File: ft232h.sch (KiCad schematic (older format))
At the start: 24 parts, among them P3 CONN_11, P4 CONN_11, P5 CONN_4, P6 CONN_4, P7 CONN_6, P8 CONN_4, Q1 CRYSTAL32-SMD, U3 FT232H, U4 USB-MINIB-5PIN_USB-MINIB, U5 93LC56CX-X/SN_SOIC8-N_MC

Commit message: crystal lib added , fixed mini-usb
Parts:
- removed Q1: CRYSTAL32-SMD, SparkFun-CRYSTAL-32KHZ-SMD, symbol CRYSTAL32-SMD
- removed U4: USB-MINIB-5PIN_USB-MINIB, symbol USB-MINIB-5PIN_USB-MINIB
- added CON1: USB-MINI-B, symbol USB-MINI-B
- added X1: 12MHz, ~, symbol CRYSTAL
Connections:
- wire segments 116 -> 107
- no-connect marks 0 -> 2
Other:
- moved on the sheet: C6
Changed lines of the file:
@@
-EESchema Schematic File Version 2  date 01-08-2013 14:43:33
+EESchema Schematic File Version 2
 LIBS:power
 LIBS:device
@@
 LIBS:93lc56c
 LIBS:cc3000-ft232h-cache
-EELAYER 27 0
+EELAYER 24 0
 EELAYER END
 $Descr A4 11693 8268
@@
 Wire Wire Line
 	4350 3500 4650 3500
-Text Label 4300 3400 0    60   ~ 0
+Text Label 4350 3400 0    60   ~ 0
 USB_D-
-Text Label 4300 3500 0    60   ~ 0
+Text Label 4350 3500 0    60   ~ 0
 USB_D+
 $Comp
@@
 	3950 5450 3950 5350
 $Comp
-L CRYSTAL32-SMD Q1
-U 1 1 51F9779C
-P 3400 4750
-F 0 "Q1" H 3500 4790 50  0000 L BNN
-F 1 "CRYSTAL32-SMD" H 3500 4650 50  0000 L BNN
-F 2 "SparkFun-CRYSTAL-32KHZ-SMD" H 3400 4900 50  0001 C CNN
-F 3 "~" H 3400 4750 60  0000 C CNN
-	1    3400 4750
-	1    0    0    -1
-$EndComp
-$Comp
 L C C7
 U 1 1 51F977A9
 P 3500 4950
-F 0 "C7" H 3500 5050 40  0000 L CNN
+F 0 "C7" H 3650 4900 40  0000 L CNN
 F 1 "27p" H 3506 4865 40  0000 L CNN
 F 2 "~" H 3538 4800 30  0000 C CNN
@@
 L C C6
 U 1 1 51F977AF
-P 3300 4950
-F 0 "C6" H 3300 5050 40  0000 L CNN
-F 1 "27p" H 3306 4865 40  0000 L CNN
-F 2 "~" H 3338 4800 30  0000 C CNN
-F 3 "~" H 3300 4950 60  0000 C CNN
-	1    3300 4950
+P 2900 4950
+F 0 "C6" H 2700 4950 40  0000 L CNN
+F 1 "27p" H 2906 4865 40  0000 L CNN
+F 2 "~" H 2938 4800 30  0000 C CNN
+F 3 "~" H 2900 4950 60  0000 C CNN
+	1    2900 4950
 	1    0    0    -1
 $EndComp
@@
 L GND #PWR041
 U 1 1 51F977BB
-P 3300 5150
-F 0 "#PWR041" H 3300 5150 30  0001 C CNN
-F 1 "GND" H 3300 5080 30  0001 C CNN
-F 2 "" H 3300 5150 60  0000 C CNN
-F 3 "" H 3300 5150 60  0000 C CNN
-	1    3300 5150
-	1    0    0    -1
-$EndComp
-Wire Wire Line
-	3300 4750 3300 4500
-Wire Wire Line
-	3300 4500 4650 4500
+P 2900 5150
+F 0 "#PWR041" H 2900 5150 30  0001 C CNN
+F 1 "GND" H 2900 5080 30  0001 C CNN
+F 2 "" H 2900 5150 60  0000 C CNN
+F 3 "" H 2900 5150 60  0000 C CNN
+	1    2900 5150
+	1    0    0    -1
+$EndComp
+Wire Wire Line
+	2900 4500 4650 4500
 Wire Wire Line
 	4650 4600 3500 4600
@@
 	-1   0    0    -1
 $EndComp
-Connection ~ 3300 4750
+Connection ~ 2900 4750
 Connection ~ 3500 4750
 Connection ~ 4350 5350
@@
 	1    0    0    -1
 $EndComp
-Wire Wire Line
-	1000 3150 1550 3150
-Wire Wire Line
-	1000 3150 1000 3300
-Wire Wire Line
-	800  2550 1250 2550
-Wire Wire Line
-	800  2700 1150 2700
-Wire Wire Line
-	800  2850 1150 2850
-Wire Wire Line
-	2150 2350 2150 3300
-Connection ~ 2150 2700
-Connection ~ 2150 3000
 $Comp
 L GND #PWR043
 U 1 1 51F9A1C1
-P 2150 3300
-F 0 "#PWR043" H 2150 3300 30  0001 C CNN
-F 1 "GND" H 2150 3230 30  0001 C CNN
-F 2 "" H 2150 3300 60  0000 C CNN
-F 3 "" H 2150 3300 60  0000 C CNN
-	1    2150 3300
-	1    0    0    -1
-$EndComp
-Connection ~ 2150 3150
-Text Label 800  2550 0    60   ~ 0
+P 2350 3300
+F 0 "#PWR043" H 2350 3300 30  0001 C CNN
+F 1 "GND" H 2350 3230 30  0001 C CNN
+F 2 "" H 2350 3300 60  0000 C CNN
+F 3 "" H 2350 3300 60  0000 C CNN
+	1    2350 3300
+	1    0    0    -1
+$EndComp
+Text Label 1250 2500 2    60   ~ 0
 VBUS
-Text Label 800  2700 0    60   ~ 0
-USB_D-
-Text Label 800  2850 0    60   ~ 0
+Text Label 1250 2800 2    60   ~ 0
 USB_D+
-$Comp
-L USB-MINIB-5PIN_USB-MINIB U4
-U 1 1 51FA0CB9
-P 1350 2950
-F 0 "U4" H 1350 2950 60  0001 C CNN
-F 1 "USB-MINIB-5PIN_USB-MINIB" H 1350 2950 60  0001 C CNN
-F 2 "" H 1350 2950 60  0000 C CNN
-F 3 "" H 1350 2950 60  0000 C CNN
-	1    1350 2950
-	1    0    0    -1
-$EndComp
-Connection ~ 1450 3150
-Wire Wire Line
-	1450 2350 2150 2350
-Connection ~ 1550 2350
-Wire Wire Line
-	1150 2700 1150 2650
-Wire Wire Line
-	1150 2650 1250 2650
-Wire Wire Line
-	1150 2850 1150 2750
-Wire Wire Line
-	1150 2750 1250 2750
-Wire Wire Line
-	1250 2950 1250 3150
-Connection ~ 1250 3150
 $Comp
 L 93LC56CX-X/SN_SOIC8-N_MC U5
 U 1 1 51FA6460
 P 2650 6800
-F 0 "U5" H 2650 6800 0   0001 C CNN
-F 1 "93LC56CX-X/SN_SOIC8-N_MC" H 2650 6800 0   0001 C CNN
+F 0 "U5" H 2650 6800 60  0001 C CNN
+F 1 "93LC56CX-X/SN_SOIC8-N_MC" H 2650 6800 60  0001 C CNN
 F 2 "" H 2650 6800 60  0000 C CNN
 F 3 "" H 2650 6800 60  0000 C CNN
@@
 	1    0    0    -1
 $EndComp
+Wire Wire Line
+	1000 3300 1000 3100
+NoConn ~ 1250 2950
+$Comp
+L CRYSTAL X1
+U 1 1 51FA7E94
+P 3200 4750
+F 0 "X1" H 3200 4900 60  0000 C CNN
+F 1 "12MHz" H 3200 4600 60  0000 C CNN
+F 2 "~" H 3200 4750 60  0000 C CNN
+F 3 "~" H 3200 4750 60  0000 C CNN
+	1    3200 4750
+	1    0    0    -1
+$EndComp
+Wire Wire Line
+	2900 4500 2900 4750
+NoConn ~ 2550 6700
+Text Label 1250 2650 2    60   ~ 0
+USB_D-
+Wire Wire Line
+	1000 3100 1250 3100
+$Comp
+L USB-MINI-B CON1
+U 1 1 51FA7F63
+P 1800 2800
+F 0 "CON1" H 1550 3250 60  0000 C CNN
+F 1 "USB-MINI-B" H 1750 2300 60  0000 C CNN
+F 2 "" H 1800 2800 60  0000 C CNN
+F 3 "" H 1800 2800 60  0000 C CNN
+	1    1800 2800
+	1    0    0    -1
+$EndComp
+Wire Wire Line
+	2350 2500 2350 3300
+Connection ~ 2350 3100
+Connection ~ 2350 2950
+Connection ~ 2350 2650
 $EndSCHEMATC

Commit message: updated
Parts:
- removed L1: INDUCTOR_SMALL, ~, symbol INDUCTOR_SMALL
- added C15: 4.7u, ~, symbol C
- added C16: 0.1, ~, symbol C
- added FB1, FB2, FB3: FILTER, ~, symbol FILTER
- added R4, R5, R6: 10K, ~, symbol R
- C12, C14: value 0.01 -> 4.7u
- C5: value 0.1 -> 0.01
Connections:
- net labels added: VCC3V3, VCCIO, VCORE
- net labels removed: +3.3V, VDEVICE
- wire segments 107 -> 122
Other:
- moved on the sheet: C5

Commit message: headers
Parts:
- removed P3, P4: CONN_11, symbol CONN_11
- removed P6, P8: CONN_4, symbol CONN_4
- added D1, D2: LED, ~, symbol LED
- added IC1: V_REG_LM1117SOT223, SparkFun-SOT223, symbol V_REG_LM1117SOT223
- added JP1, JP2, JP3, JP4: JUMPER, ~, symbol JUMPER
- added P3, P4: CONN_13, symbol CONN_13
- added R10, R9: 10K, ~, symbol R
- added R11, R12: R, ~, symbol R
- added R7, R8: 12K, ~, symbol R
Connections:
- net labels added: +3.3V
- net labels removed: SCL, SDA, TCK, TDI, TDO, TMS, VCCIO, V_OUT
- wire segments 122 -> 134
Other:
- moved on the sheet: P5

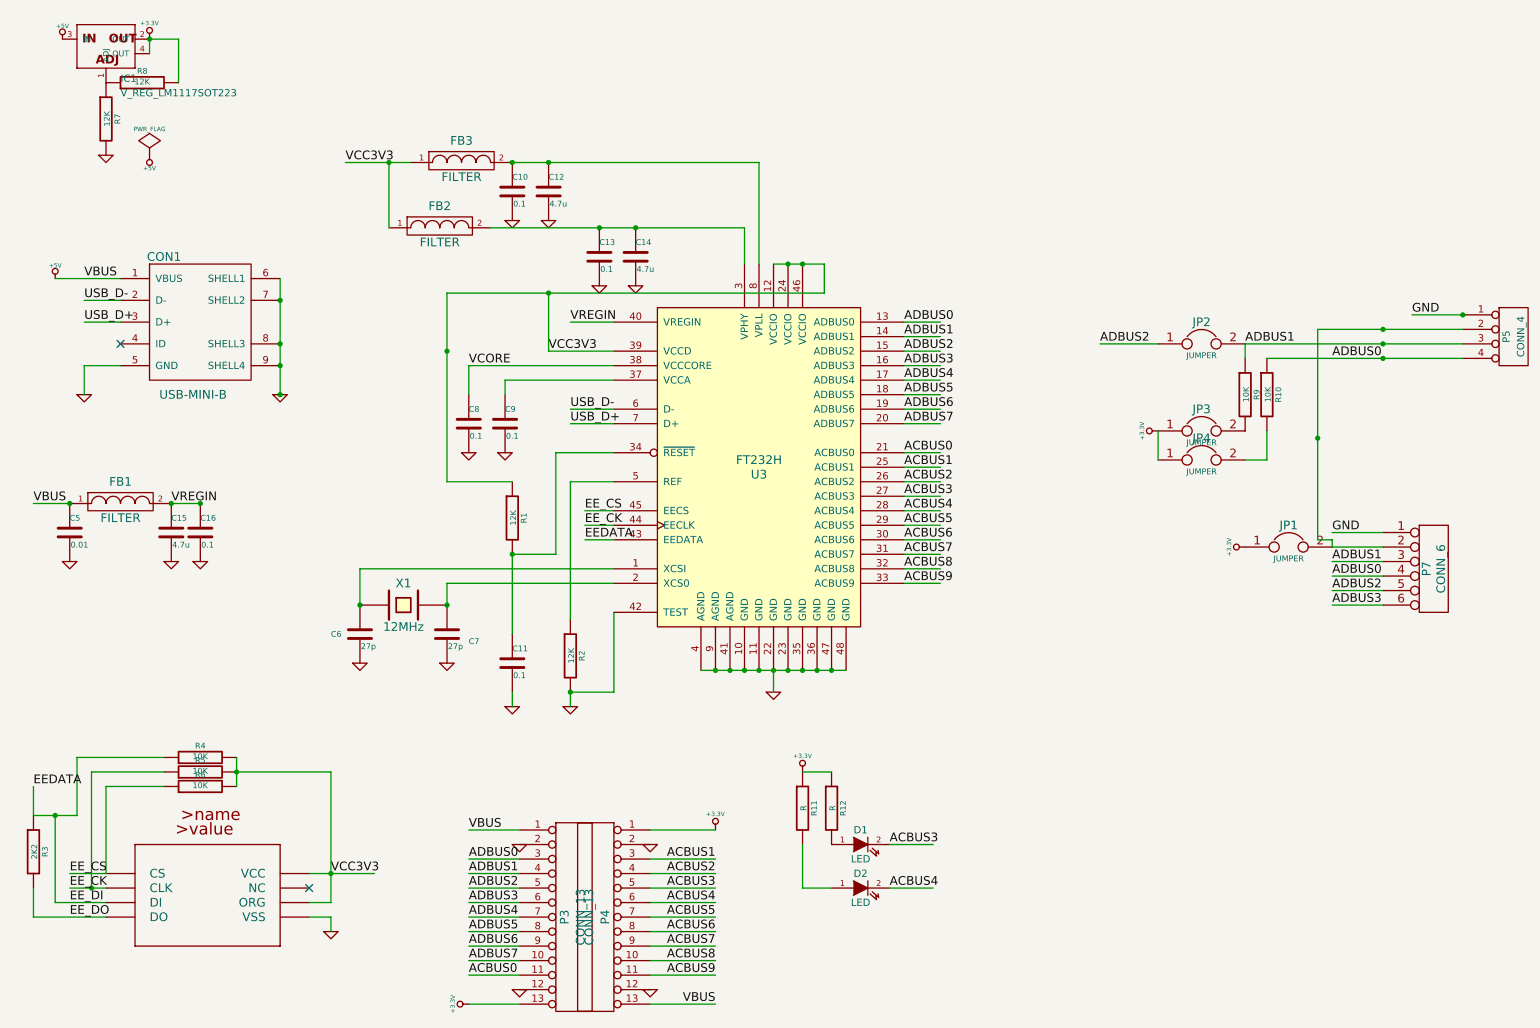
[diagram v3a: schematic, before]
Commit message: faltam 20 ligaoes e caps mal
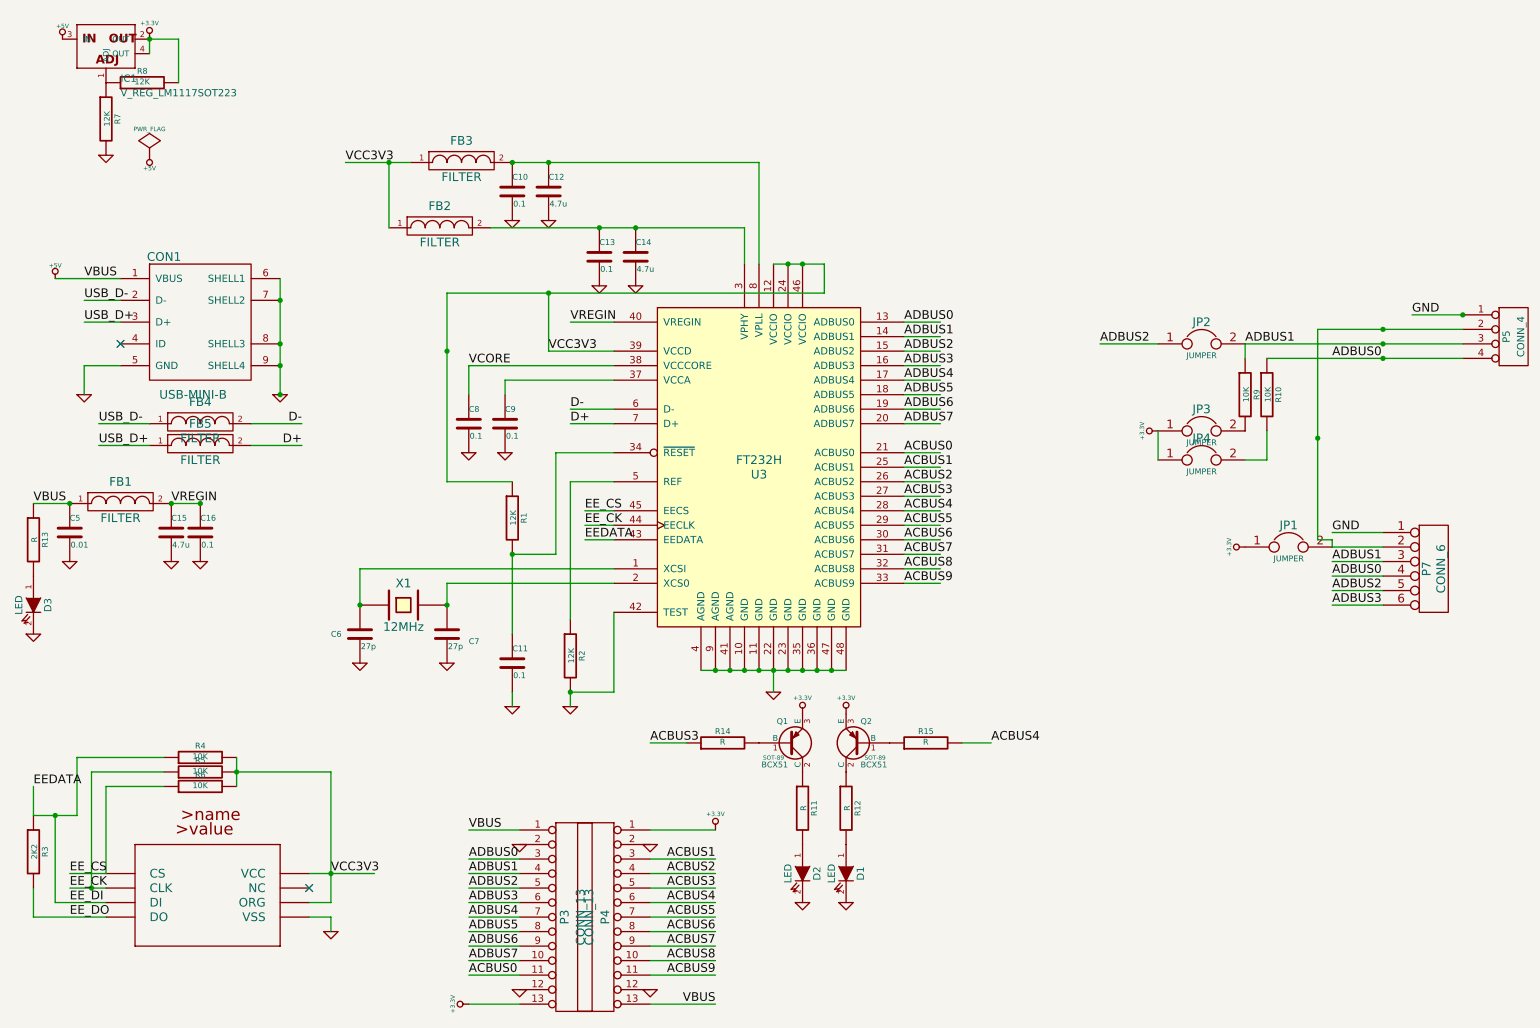
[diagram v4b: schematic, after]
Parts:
- added D3: LED, ~, symbol LED
- added FB4, FB5: FILTER, ~, symbol FILTER
- added Q1, Q2: BCX51, SOT-89, symbol BCX51
- added R13, R14, R15: R, ~, symbol R
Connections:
- net labels added: D+, D-
- wire segments 134 -> 135
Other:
- moved on the sheet: D1, D2, R12
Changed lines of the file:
@@
-EESchema Schematic File Version 2  date 02-08-2013 15:57:30
+EESchema Schematic File Version 2  date 02-08-2013 23:29:06
 LIBS:power
 LIBS:device
@@
 $EndComp
 Text Label 4350 3400 0    60   ~ 0
-USB_D-
+D-
 Text Label 4350 3500 0    60   ~ 0
-USB_D+
+D+
 $Comp
 L C C5
@@
 L LED D1
 U 1 1 51FBC5BE
-P 6350 6400
-F 0 "D1" H 6350 6500 50  0000 C CNN
-F 1 "LED" H 6350 6300 50  0000 C CNN
-F 2 "~" H 6350 6400 60  0000 C CNN
-F 3 "~" H 6350 6400 60  0000 C CNN
-	1    6350 6400
-	1    0    0    -1
-$EndComp
-$Comp
-L LED D2
-U 1 1 51FBC5CD
-P 6350 6700
-F 0 "D2" H 6350 6800 50  0000 C CNN
-F 1 "LED" H 6350 6600 50  0000 C CNN
-F 2 "~" H 6350 6700 60  0000 C CNN
-F 3 "~" H 6350 6700 60  0000 C CNN
-	1    6350 6700
-	1    0    0    -1
-$EndComp
-Wire Wire Line
-	6850 6400 6550 6400
-Wire Wire Line
-	6850 6700 6550 6700
-Text Label 6550 6400 0    60   ~ 0
-ACBUS3
-Text Label 6550 6700 0    60   ~ 0
-ACBUS4
+P 6250 6600
+F 0 "D1" H 6250 6700 50  0000 C CNN
+F 1 "LED" H 6250 6500 50  0000 C CNN
+F 2 "~" H 6250 6600 60  0000 C CNN
+F 3 "~" H 6250 6600 60  0000 C CNN
+	1    6250 6600
+	0    1    1    0
+$EndComp
 $Comp
 L R R11
@@
 L R R12
 U 1 1 51FBC766
-P 6150 6150
-F 0 "R12" V 6230 6150 40  0000 C CNN
-F 1 "R" V 6157 6151 40  0000 C CNN
-F 2 "~" V 6080 6150 30  0000 C CNN
-F 3 "~" H 6150 6150 30  0000 C CNN
-	1    6150 6150
-	1    0    0    -1
-$EndComp
-Wire Wire Line
-	5950 6400 5950 6700
-Wire Wire Line
-	5950 6700 6150 6700
-$Comp
-L +3.3V #PWR054
-U 1 1 51FBC8EC
-P 5950 5900
-F 0 "#PWR054" H 5950 5860 30  0001 C CNN
-F 1 "+3.3V" H 5950 6010 30  0000 C CNN
-F 2 "" H 5950 5900 60  0000 C CNN
-F 3 "" H 5950 5900 60  0000 C CNN
-	1    5950 5900
-	1    0    0    -1
-$EndComp
-Wire Wire Line
-	5950 5900 6150 5900
+P 6250 6150
+F 0 "R12" V 6330 6150 40  0000 C CNN
+F 1 "R" V 6257 6151 40  0000 C CNN
+F 2 "~" V 6180 6150 30  0000 C CNN
+F 3 "~" H 6250 6150 30  0000 C CNN
+	1    6250 6150
+	1    0    0    -1
+$EndComp
 Text Label 3650 7100 0    60   ~ 0
 ADBUS6
 $Comp
-L GND #PWR055
+L GND #PWR054
 U 1 1 51FBCDF7
 P 4900 6400
-F 0 "#PWR055" H 4900 6400 30  0001 C CNN
+F 0 "#PWR054" H 4900 6400 30  0001 C CNN
 F 1 "GND" H 4900 6330 30  0001 C CNN
 F 2 "" H 4900 6400 60  0000 C CNN
@@
 ACBUS4
 $Comp
-L GND #PWR056
+L GND #PWR055
 U 1 1 51FBCE03
 P 4900 7400
-F 0 "#PWR056" H 4900 7400 30  0001 C CNN
+F 0 "#PWR055" H 4900 7400 30  0001 C CNN
 F 1 "GND" H 4900 7330 30  0001 C CNN
 F 2 "" H 4900 7400 60  0000 C CNN
@@
 $EndComp
 $Comp
-L GND #PWR057
+L GND #PWR056
 U 1 1 51FBCE09
 P 4000 6400
-F 0 "#PWR057" H 4000 6400 30  0001 C CNN
+F 0 "#PWR056" H 4000 6400 30  0001 C CNN
 F 1 "GND" H 4000 6330 30  0001 C CNN
 F 2 "" H 4000 6400 60  0000 C CNN
@@
 Text Label 4350 2800 0    60   ~ 0
 VREGIN
+$Comp
+L FILTER FB4
+U 1 1 51FC0357
+P 1800 3500
+F 0 "FB4" H 1800 3650 60  0000 C CNN
+F 1 "FILTER" H 1800 3400 60  0000 C CNN
+F 2 "~" H 1800 3500 60  0000 C CNN
+F 3 "~" H 1800 3500 60  0000 C CNN
+	1    1800 3500
+	1    0    0    -1
+$EndComp
+$Comp
+L FILTER FB5
+U 1 1 51FC035D
+P 1800 3650
+F 0 "FB5" H 1800 3800 60  0000 C CNN
+F 1 "FILTER" H 1800 3550 60  0000 C CNN
+F 2 "~" H 1800 3650 60  0000 C CNN
+F 3 "~" H 1800 3650 60  0000 C CNN
+	1    1800 3650
+	1    0    0    -1
+$EndComp
+Wire Wire Line
+	1100 3500 1450 3500
+Wire Wire Line
+	1100 3650 1450 3650
+Wire Wire Line
+	2500 3500 2150 3500
+Wire Wire Line
+	2500 3650 2150 3650
+Text Label 2500 3500 2    60   ~ 0
+D-
+Text Label 2500 3650 2    60   ~ 0
+D+
+Text Label 1100 3500 0    60   ~ 0
+USB_D-
+Text Label 1100 3650 0    60   ~ 0
+USB_D+
+$Comp
+L R R13
+U 1 1 51FC143C
+P 650 4300
+F 0 "R13" V 730 4300 40  0000 C CNN
+F 1 "R" V 657 4301 40  0000 C CNN
+F 2 "~" V 580 4300 30  0000 C CNN
+F 3 "~" H 650 4300 30  0000 C CNN
+	1    650  4300
+	1    0    0    -1
+$EndComp
+$Comp
+L LED D3
+U 1 1 51FC1446
+P 650 4750
+F 0 "D3" H 650 4850 50  0000 C CNN
+F 1 "LED" H 650 4650 50  0000 C CNN
+F 2 "~" H 650 4750 60  0000 C CNN
+F 3 "~" H 650 4750 60  0000 C CNN
+	1    650  4750
+	0    1    1    0
+$EndComp
+$Comp
+L GND #PWR057
+U 1 1 51FC144D
+P 650 4950
+F 0 "#PWR057" H 650 4950 30  0001 C CNN
+F 1 "GND" H 650 4880 30  0001 C CNN
+F 2 "" H 650 4950 60  0000 C CNN
+F 3 "" H 650 4950 60  0000 C CNN
+	1    650  4950
+	1    0    0    -1
+$EndComp
+$Comp
+L LED D2
+U 1 1 51FBC5CD
+P 5950 6600
+F 0 "D2" H 5950 6700 50  0000 C CNN
+F 1 "LED" H 5950 6500 50  0000 C CNN
+F 2 "~" H 5950 6600 60  0000 C CNN
+F 3 "~" H 5950 6600 60  0000 C CNN
+	1    5950 6600
+	0    1    1    0
+$EndComp
+$Comp
+L GND #PWR058
+U 1 1 51FC154D
+P 5950 6800
+F 0 "#PWR058" H 5950 6800 30  0001 C CNN
+F 1 "GND" H 5950 6730 30  0001 C CNN
+F 2 "" H 5950 6800 60  0000 C CNN
+F 3 "" H 5950 6800 60  0000 C CNN
+	1    5950 6800
+	1    0    0    -1
+$EndComp
+$Comp
+L GND #PWR059
+U 1 1 51FC1553
+P 6250 6800
+F 0 "#PWR059" H 6250 6800 30  0001 C CNN
+F 1 "GND" H 6250 6730 30  0001 C CNN
+F 2 "" H 6250 6800 60  0000 C CNN
+F 3 "" H 6250 6800 60  0000 C CNN
+	1    6250 6800
+	1    0    0    -1
+$EndComp
+$Comp
+L +3.3V #PWR060
+U 1 1 51FC1559
+P 6250 5500
+F 0 "#PWR060" H 6250 5460 30  0001 C CNN
+F 1 "+3.3V" H 6250 5610 30  0000 C CNN
+F 2 "" H 6250 5500 60  0000 C CNN
+F 3 "" H 6250 5500 60  0000 C CNN
+	1    6250 5500
+	1    0    0    -1
+$EndComp
+$Comp
+L +3.3V #PWR061
+U 1 1 51FC155F
+P 5950 5500
+F 0 "#PWR061" H 5950 5460 30  0001 C CNN
+F 1 "+3.3V" H 5950 5610 30  0000 C CNN
+F 2 "" H 5950 5500 60  0000 C CNN
+F 3 "" H 5950 5500 60  0000 C CNN
+	1    5950 5500
+	1    0    0    -1
+$EndComp
+$Comp
+L R R14
+U 1 1 51FC2884
+P 5400 5700
+F 0 "R14" V 5480 5700 40  0000 C CNN
+F 1 "R" V 5407 5701 40  0000 C CNN
+F 2 "~" V 5330 5700 30  0000 C CNN
+F 3 "~" H 5400 5700 30  0000 C CNN
+	1    5400 5700
+	0    -1   -1   0
+$EndComp
+$Comp
+L R R15
+U 1 1 51FC2894
+P 6800 5700
+F 0 "R15" V 6880 5700 40  0000 C CNN
+F 1 "R" V 6807 5701 40  0000 C CNN
+F 2 "~" V 6730 5700 30  0000 C CNN
+F 3 "~" H 6800 5700 30  0000 C CNN
+	1    6800 5700
+	0    -1   -1   0
+$EndComp
+Wire Wire Line
+	4900 5700 5150 5700
+Wire Wire Line
+	7250 5700 7050 5700
+Text Label 4900 5700 0    60   ~ 0
+ACBUS3
+Text Label 7250 5700 0    60   ~ 0
+ACBUS4
+$Comp
+L BCX51 Q2
+U 1 1 51FC3299
+P 6350 5700
+F 0 "Q2" H 6350 5551 40  0000 R CNN
+F 1 "BCX51" H 6350 5850 40  0000 R CNN
+F 2 "SOT-89" H 6250 5802 29  0000 C CNN
+F 3 "~" H 6350 5700 60  0000 C CNN
+	1    6350 5700
+	-1   0    0    1
+$EndComp
+$Comp
+L BCX51 Q1
+U 1 1 51FC32A6
+P 5850 5700
+F 0 "Q1" H 5850 5551 40  0000 R CNN
+F 1 "BCX51" H 5850 5850 40  0000 R CNN
+F 2 "SOT-89" H 5750 5802 29  0000 C CNN
+F 3 "~" H 5850 5700 60  0000 C CNN
+	1    5850 5700
+	1    0    0    1
+$EndComp
 $EndSCHEMATC

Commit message: ftdi pronto(versao beta) + breakout
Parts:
- added C17: 0.1, ~, symbol C
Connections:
- wire segments 135 -> 136
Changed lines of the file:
@@
-EESchema Schematic File Version 2  date 02-08-2013 23:29:06
+EESchema Schematic File Version 2  date 03-08-2013 18:34:25
 LIBS:power
 LIBS:device
@@
 $Descr A4 11693 8268
 encoding utf-8
-Sheet 3 3
+Sheet 3 4
 Title ""
-Date "2 aug 2013"
+Date "3 aug 2013"
 Rev ""
 Comp ""
@@
 	1    0    0    1
 $EndComp
+$Comp
+L C C17
+U 1 1 51FD3F0C
+P 3000 6800
+F 0 "C17" H 3000 6900 40  0000 L CNN
+F 1 "0.1" H 3006 6715 40  0000 L CNN
+F 2 "~" H 3038 6650 30  0000 C CNN
+F 3 "~" H 3000 6800 60  0000 C CNN
+	1    3000 6800
+	1    0    0    -1
+$EndComp
+Wire Wire Line
+	3000 7000 2700 7000
 $EndSCHEMATC

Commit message: ftdi pronto(versao beta) + breakout
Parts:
- removed FB4, FB5: FILTER, ~, symbol FILTER
- added P6: CONN_1, symbol CONN_1
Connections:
- net labels removed: D+, D-
- wire segments 136 -> 132
